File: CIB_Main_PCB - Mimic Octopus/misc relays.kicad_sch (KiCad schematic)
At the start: 7 parts, among them U3 ULN2803A, U4 MCP23017_SO, U6 ULN2803A, U7 MCP23017_SO, U8 ULN2803A

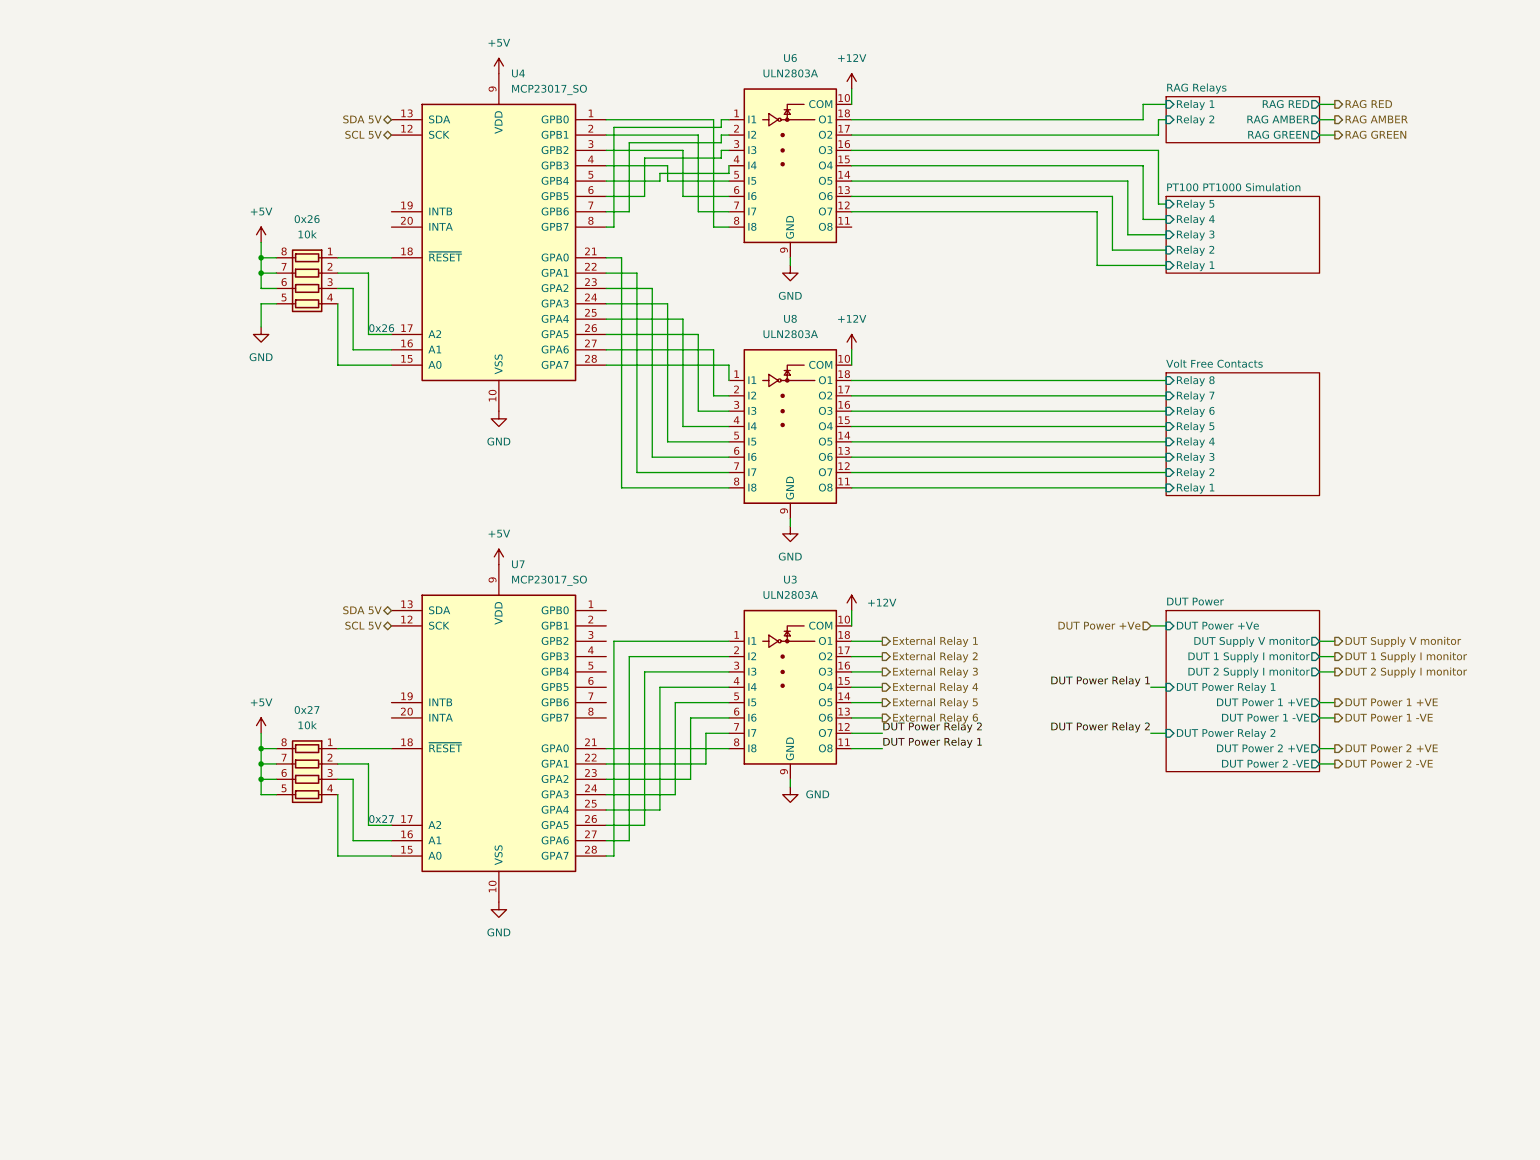
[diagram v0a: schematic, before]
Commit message: added version resistors
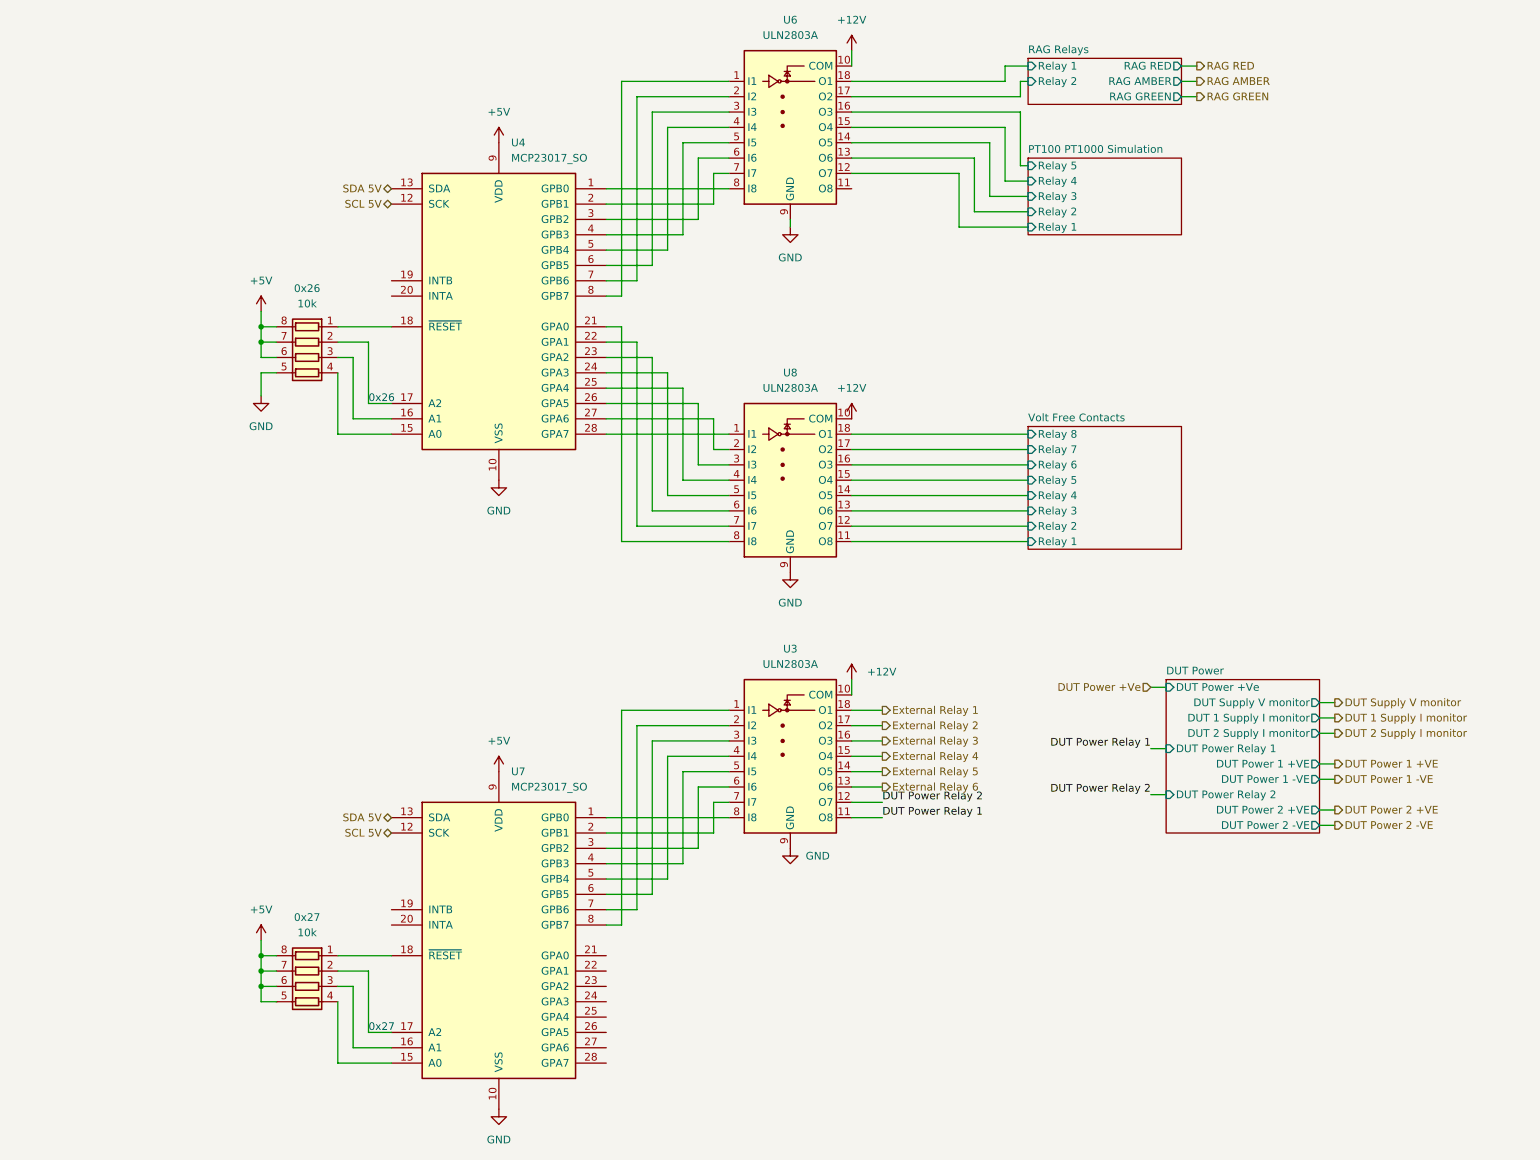
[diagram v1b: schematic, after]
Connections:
- net at U7.1 (GPB0): now also U3.8 (I8)
- net at U7.2 (GPB1): now also U3.7 (I7)
- net at U7.21 (GPA0): no longer U3.8 (I8)
- net at U7.22 (GPA1): no longer U3.7 (I7)
- net at U7.23 (GPA2): no longer U3.6 (I6)
- net at U7.24 (GPA3): no longer U3.5 (I5)
- net at U7.25 (GPA4): no longer U3.4 (I4)
- net at U7.26 (GPA5): no longer U3.3 (I3)
- net at U7.27 (GPA6): no longer U3.2 (I2)
- net at U7.28 (GPA7): no longer U3.1 (I1)
- net at U7.3 (GPB2): now also U3.6 (I6)
- net at U7.4 (GPB3): now also U3.5 (I5)
- net at U7.5 (GPB4): now also U3.4 (I4)
- net at U7.6 (GPB5): now also U3.3 (I3)
- net at U7.7 (GPB6): now also U3.2 (I2)
- net at U7.8 (GPB7): now also U3.1 (I1)
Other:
- moved on the sheet: 0x26, 0x27, U3, U4, U6, U7, U8

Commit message: added changes
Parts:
- renumbered 0x26 to 0x1, 0x27 to 0x2, U6 to U3, U8 to U5, U3 to U6
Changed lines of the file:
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@@
   (symbol (lib_id "Device:R_Pack04") (at 67.31 175.26 90) (mirror x) (unit 1)
     (in_bom yes) (on_board yes) (fields_autoplaced)
-    (property "Reference" "0x27" (id 0) (at 67.31 163.83 90))
+    (property "Reference" "0x2" (id 0) (at 67.31 163.83 90))
     (property "Value" "10k" (id 1) (at 67.31 166.37 90))
     (property "Footprint" "Resistor_SMD:R_Array_Convex_4x1206" (id 2) (at 67.31 182.245 90)
@@
   (symbol (lib_id "power:+12V") (at 157.48 81.28 0) (unit 1)
     (in_bom yes) (on_board yes) (fields_autoplaced)
-    (property "Reference" "#PWR097" (id 0) (at 157.48 85.09 0)
+    (property "Reference" "#PWR084" (id 0) (at 157.48 85.09 0)
       (effects (font (size 1.27 1.27)) hide)
     )
@@
   (symbol (lib_id "power:GND") (at 59.69 77.47 0) (unit 1)
     (in_bom yes) (on_board yes) (fields_autoplaced)
-    (property "Reference" "#PWR0117" (id 0) (at 59.69 83.82 0)
+    (property "Reference" "#PWR083" (id 0) (at 59.69 83.82 0)
       (effects (font (size 1.27 1.27)) hide)
     )
@@
   (symbol (lib_id "Transistor_Array:ULN2803A") (at 147.32 88.9 0) (unit 1)
     (in_bom yes) (on_board yes) (fields_autoplaced)
-    (property "Reference" "U8" (id 0) (at 147.32 73.66 0))
+    (property "Reference" "U5" (id 0) (at 147.32 73.66 0))
     (property "Value" "ULN2803A" (id 1) (at 147.32 76.2 0))
     (property "Footprint" "Package_DIP:DIP-18_W7.62mm_LongPads" (id 2) (at 148.59 105.41 0)
@@
   (symbol (lib_id "Device:R_Pack04") (at 67.31 71.12 90) (mirror x) (unit 1)
     (in_bom yes) (on_board yes) (fields_autoplaced)
-    (property "Reference" "0x26" (id 0) (at 67.31 59.69 90))
+    (property "Reference" "0x1" (id 0) (at 67.31 59.69 90))
     (property "Value" "10k" (id 1) (at 67.31 62.23 90))
     (property "Footprint" "Resistor_SMD:R_Array_Convex_4x1206" (id 2) (at 67.31 78.105 90)
@@
   (symbol (lib_id "Transistor_Array:ULN2803A") (at 147.32 30.48 0) (unit 1)
     (in_bom yes) (on_board yes) (fields_autoplaced)
-    (property "Reference" "U6" (id 0) (at 147.32 15.24 0))
+    (property "Reference" "U3" (id 0) (at 147.32 15.24 0))
     (property "Value" "ULN2803A" (id 1) (at 147.32 17.78 0))
     (property "Footprint" "Package_DIP:DIP-18_W7.62mm_LongPads" (id 2) (at 148.59 46.99 0)
@@
   (symbol (lib_id "power:+5V") (at 99.06 35.56 0) (unit 1)
     (in_bom yes) (on_board yes) (fields_autoplaced)
-    (property "Reference" "#PWR0112" (id 0) (at 99.06 39.37 0)
+    (property "Reference" "#PWR080" (id 0) (at 99.06 39.37 0)
       (effects (font (size 1.27 1.27)) hide)
     )
@@
   (symbol (lib_id "power:GND") (at 147.32 49.53 0) (unit 1)
     (in_bom yes) (on_board yes) (fields_autoplaced)
-    (property "Reference" "#PWR094" (id 0) (at 147.32 55.88 0)
+    (property "Reference" "#PWR081" (id 0) (at 147.32 55.88 0)
       (effects (font (size 1.27 1.27)) hide)
     )
@@
   (symbol (lib_id "power:GND") (at 99.06 195.58 0) (unit 1)
     (in_bom yes) (on_board yes) (fields_autoplaced)
-    (property "Reference" "#PWR0114" (id 0) (at 99.06 201.93 0)
+    (property "Reference" "#PWR091" (id 0) (at 99.06 201.93 0)
       (effects (font (size 1.27 1.27)) hide)
     )
@@
   (symbol (lib_id "power:+12V") (at 157.48 20.32 0) (unit 1)
     (in_bom yes) (on_board yes) (fields_autoplaced)
-    (property "Reference" "#PWR085" (id 0) (at 157.48 24.13 0)
+    (property "Reference" "#PWR079" (id 0) (at 157.48 24.13 0)
       (effects (font (size 1.27 1.27)) hide)
     )
@@
   (symbol (lib_id "power:+5V") (at 99.06 139.7 0) (unit 1)
     (in_bom yes) (on_board yes)
-    (property "Reference" "#PWR0116" (id 0) (at 99.06 143.51 0)
+    (property "Reference" "#PWR088" (id 0) (at 99.06 143.51 0)
       (effects (font (size 1.27 1.27)) hide)
     )
@@
   (symbol (lib_id "power:+5V") (at 59.69 167.64 0) (unit 1)
     (in_bom yes) (on_board yes)
-    (property "Reference" "#PWR0113" (id 0) (at 59.69 171.45 0)
+    (property "Reference" "#PWR090" (id 0) (at 59.69 171.45 0)
       (effects (font (size 1.27 1.27)) hide)
     )
@@
   (symbol (lib_id "Transistor_Array:ULN2803A") (at 147.32 134.62 0) (unit 1)
     (in_bom yes) (on_board yes) (fields_autoplaced)
-    (property "Reference" "U3" (id 0) (at 147.32 119.38 0))
+    (property "Reference" "U6" (id 0) (at 147.32 119.38 0))
     (property "Value" "ULN2803A" (id 1) (at 147.32 121.92 0))
     (property "Footprint" "Package_DIP:DIP-18_W7.62mm_LongPads" (id 2) (at 148.59 151.13 0)
@@
   (symbol (lib_id "power:GND") (at 147.32 152.4 0) (unit 1)
     (in_bom yes) (on_board yes) (fields_autoplaced)
-    (property "Reference" "#PWR0375" (id 0) (at 147.32 158.75 0)
+    (property "Reference" "#PWR089" (id 0) (at 147.32 158.75 0)
       (effects (font (size 1.27 1.27)) hide)
     )
@@
   (symbol (lib_id "power:GND") (at 99.06 91.44 0) (unit 1)
     (in_bom yes) (on_board yes) (fields_autoplaced)
-    (property "Reference" "#PWR0115" (id 0) (at 99.06 97.79 0)
+    (property "Reference" "#PWR085" (id 0) (at 99.06 97.79 0)
       (effects (font (size 1.27 1.27)) hide)
     )
@@
   (symbol (lib_id "power:+5V") (at 59.69 63.5 0) (unit 1)
     (in_bom yes) (on_board yes)
-    (property "Reference" "#PWR0121" (id 0) (at 59.69 67.31 0)
+    (property "Reference" "#PWR082" (id 0) (at 59.69 67.31 0)
       (effects (font (size 1.27 1.27)) hide)
     )
@@
   (symbol (lib_id "power:+12V") (at 157.48 124.46 0) (unit 1)
     (in_bom yes) (on_board yes) (fields_autoplaced)
-    (property "Reference" "#PWR0374" (id 0) (at 157.48 128.27 0)
+    (property "Reference" "#PWR087" (id 0) (at 157.48 128.27 0)
       (effects (font (size 1.27 1.27)) hide)
     )
@@
   (symbol (lib_id "power:GND") (at 147.32 106.68 0) (unit 1)
     (in_bom yes) (on_board yes) (fields_autoplaced)
-    (property "Reference" "#PWR0101" (id 0) (at 147.32 113.03 0)
-      (effects (font (size 1.27 1.27)) hide)
-    )
+    (property "Reference" "#PWR086" (id 0) (at 147.32 113.03 0)
+      (effects (font (size 1.27 1.27)) hide)
+    )

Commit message: V0.1 PCB to be sent out
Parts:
- removed 0x1, 0x2: 10k, Resistor_SMD:R_Array_Convex_4x1206, symbol Device:R_Pack04
- removed U4, U7: MCP23017_SO, Package_SO:SOIC-28W_7.5x17.9mm_P1.27mm, symbol Interface_Expansion:MCP23017_SO
- added U4, U7, U8: 74HC595, Package_DIP:DIP-16_W7.62mm_LongPads, symbol 74xx:74HC595
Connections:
- net +5V: now also U4.10 (~{SRCLR}), U4.16 (VCC), U7.10 (~{SRCLR}), U7.16 (VCC), U8.10 (~{SRCLR}), U8.16 (VCC)
- net DUT Power Relay 1: now also U3.11 (O8); no longer U6.11 (O8)
- net DUT Power Relay 2: now also U3.12 (O7); no longer U6.12 (O7)
- net External Relay 1: now also U6.16 (O3); no longer U6.18 (O1)
- net External Relay 2: now also U6.15 (O4); no longer U6.17 (O2)
- net External Relay 3: now also U6.14 (O5); no longer U6.16 (O3)
- net External Relay 4: now also U6.13 (O6); no longer U6.15 (O4)
- net External Relay 5: now also U6.12 (O7); no longer U6.14 (O5)
- net External Relay 6: now also U6.11 (O8); no longer U6.13 (O6)
- net GND: now also U4.13 (~{OE}), U4.8 (GND), U7.13 (~{OE}), U7.8 (GND), U8.13 (~{OE}), U8.8 (GND)
- net PT100 PT1000 Simulation/Relay 1: now also U3.16 (O3); no longer U3.12 (O7)
- net PT100 PT1000 Simulation/Relay 2: now also U3.17 (O2); no longer U3.13 (O6)
- net PT100 PT1000 Simulation/Relay 3: now also U3.15 (O4); no longer U3.14 (O5)
- net PT100 PT1000 Simulation/Relay 4: now also U3.14 (O5); no longer U3.15 (O4)
- net PT100 PT1000 Simulation/Relay 5: now also U3.13 (O6); no longer U3.16 (O3)
- net RAG Relays/Relay 1: now also U6.17 (O2); no longer U3.18 (O1)
- net RAG Relays/Relay 2: now also U6.18 (O1); no longer U3.17 (O2)
- net at U5.1 (I1): now also U7.7 (QH)
- net at U5.2 (I2): now also U7.6 (QG)
- net at U5.3 (I3): now also U7.5 (QF)
- net at U5.4 (I4): now also U7.4 (QE)
- net at U5.5 (I5): now also U7.3 (QD)
- net at U5.6 (I6): now also U7.2 (QC)
- net at U5.7 (I7): now also U7.1 (QB)
- net at U5.8 (I8): now also U7.15 (QA)
- net at U6.8 (I8): now also U8.15 (QA)
- net at U6.7 (I7): now also U8.1 (QB)
- net at U6.6 (I6): now also U8.2 (QC)
- net at U6.5 (I5): now also U8.3 (QD)
- net at U6.4 (I4): now also U8.4 (QE)
- net at U6.3 (I3): now also U8.5 (QF)
- net at U6.2 (I2): now also U8.6 (QG)
- net at U6.1 (I1): now also U8.7 (QH)
- net at U3.1 (I1): now also U4.7 (QH)
- net at U3.2 (I2): now also U4.6 (QG)
- net at U3.3 (I3): now also U4.5 (QF)
- net at U3.4 (I4): now also U4.4 (QE)
- net at U3.5 (I5): now also U4.3 (QD)
- net at U3.6 (I6): now also U4.2 (QC)
- net at U3.7 (I7): now also U4.1 (QB)
- net at U3.8 (I8): now also U4.15 (QA)
- new net: U7.9 (QH'), U8.14 (SER)
- new net Clock: U4.11 (SRCLK), U7.11 (SRCLK), U8.11 (SRCLK)
- new net DIN: U7.14 (SER)
- new net DOUT: U4.9 (QH')
- new net External Relay 7: U3.18 (O1)
- new net Latch: U4.12 (RCLK), U7.12 (RCLK), U8.12 (RCLK)
- new net data: U4.14 (SER), U8.9 (QH')
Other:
- note removed: "0x26"
- note removed: "0x27"
- moved on the sheet: U3, U5, U6

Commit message: BoM
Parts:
- U3, U5, U6: Height (none) -> 5; Mouser # (none) -> 511-ULN2803A; Mouser Part Number 511-ULN2803A -> (none)
- U4, U7, U8: Height (none) -> 5
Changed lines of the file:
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@@
+      (effects (font (size 1.27 1.27)) hide)
+    )
+    (property "Manufacturer" "STMicroelectronics" (id 7) (at 85.09 106.68 0)
+      (effects (font (size 1.27 1.27)) hide)
+    )
+    (property "Manufacturer #" "ULN2803A" (id 5) (at 85.09 106.68 0)
       (effects (font (size 1.27 1.27)) hide)
     )
@@
       (effects (font (size 1.27 1.27)) hide)
     )
-    (property "Manufacturer #" "ULN2803A" (id 5) (at 85.09 106.68 0)
-      (effects (font (size 1.27 1.27)) hide)
-    )
-    (property "Manufacturere" "" (id 6) (at 85.09 106.68 0)
-      (effects (font (size 1.27 1.27)) hide)
-    )
-    (property "Manufacturer" "STMicroelectronics" (id 7) (at 85.09 106.68 0)
-      (effects (font (size 1.27 1.27)) hide)
-    )
-    (property "Mouser #" "" (id 8) (at 85.09 106.68 0)
-      (effects (font (size 1.27 1.27)) hide)
-    )
-    (property "Mouser Part Number" "511-ULN2803A" (id 9) (at 85.09 106.68 0)
+    (property "Mouser #" "511-ULN2803A" (id 8) (at 85.09 106.68 0)
+      (effects (font (size 1.27 1.27)) hide)
+    )
+    (property "Mouser Part Number" "" (id 9) (at 85.09 106.68 0)
+      (effects (font (size 1.27 1.27)) hide)
+    )
+    (property "Height" "5" (id 10) (at 85.09 106.68 0)
       (effects (font (size 1.27 1.27)) hide)
     )
@@
       (effects (font (size 1.27 1.27)) hide)
     )
+    (property "Manufacturer" "STMicroelectronics" (id 7) (at 85.09 48.26 0)
+      (effects (font (size 1.27 1.27)) hide)
+    )
+    (property "Manufacturer #" "ULN2803A" (id 5) (at 85.09 48.26 0)
+      (effects (font (size 1.27 1.27)) hide)
+    )
     (property "DigiKey #" "497-2356-5-ND" (id 4) (at 85.09 48.26 0)
       (effects (font (size 1.27 1.27)) hide)
     )
-    (property "Manufacturer #" "ULN2803A" (id 5) (at 85.09 48.26 0)
-      (effects (font (size 1.27 1.27)) hide)
-    )
-    (property "Manufacturere" "" (id 6) (at 85.09 48.26 0)
-      (effects (font (size 1.27 1.27)) hide)
-    )
-    (property "Manufacturer" "STMicroelectronics" (id 7) (at 85.09 48.26 0)
-      (effects (font (size 1.27 1.27)) hide)
-    )
-    (property "Mouser #" "" (id 8) (at 85.09 48.26 0)
-      (effects (font (size 1.27 1.27)) hide)
-    )
-    (property "Mouser Part Number" "511-ULN2803A" (id 9) (at 85.09 48.26 0)
+    (property "Mouser #" "511-ULN2803A" (id 8) (at 85.09 48.26 0)
+      (effects (font (size 1.27 1.27)) hide)
+    )
+    (property "Mouser Part Number" "" (id 9) (at 85.09 48.26 0)
+      (effects (font (size 1.27 1.27)) hide)
+    )
+    (property "Height" "5" (id 10) (at 85.09 48.26 0)
       (effects (font (size 1.27 1.27)) hide)
     )
@@
       (effects (font (size 1.27 1.27)) hide)
     )
+    (property "Height" "5" (id 4) (at 44.45 93.98 0)
+      (effects (font (size 1.27 1.27)) hide)
+    )
     (pin "1")
     (pin "10")
@@
       (effects (font (size 1.27 1.27)) hide)
     )
+    (property "Height" "5" (id 4) (at 44.45 35.56 0)
+      (effects (font (size 1.27 1.27)) hide)
+    )
     (pin "1")
     (pin "10")
@@
     )
     (property "Datasheet" "http://www.ti.com/lit/ds/symlink/sn74hc595.pdf" (id 3) (at 44.45 143.51 0)
+      (effects (font (size 1.27 1.27)) hide)
+    )
+    (property "Height" "5" (id 4) (at 44.45 143.51 0)
       (effects (font (size 1.27 1.27)) hide)
     )
@@
       (effects (font (size 1.27 1.27)) hide)
     )
+    (property "Manufacturer" "STMicroelectronics" (id 7) (at 85.09 156.21 0)
+      (effects (font (size 1.27 1.27)) hide)
+    )
+    (property "Manufacturer #" "ULN2803A" (id 5) (at 85.09 156.21 0)
+      (effects (font (size 1.27 1.27)) hide)
+    )
     (property "DigiKey #" "497-2356-5-ND" (id 4) (at 85.09 156.21 0)
       (effects (font (size 1.27 1.27)) hide)
     )
-    (property "Manufacturer #" "ULN2803A" (id 5) (at 85.09 156.21 0)
-      (effects (font (size 1.27 1.27)) hide)
-    )
-    (property "Manufacturere" "" (id 6) (at 85.09 156.21 0)
-      (effects (font (size 1.27 1.27)) hide)
-    )
-    (property "Manufacturer" "STMicroelectronics" (id 7) (at 85.09 156.21 0)
-      (effects (font (size 1.27 1.27)) hide)
-    )
-    (property "Mouser #" "" (id 8) (at 85.09 156.21 0)
-      (effects (font (size 1.27 1.27)) hide)
-    )
-    (property "Mouser Part Number" "511-ULN2803A" (id 9) (at 85.09 156.21 0)
-      (effects (font (size 1.27 1.27)) hide)
-    )
+    (property "Mouser #" "511-ULN2803A" (id 8) (at 85.09 156.21 0)
+      (effects (font (size 1.27 1.27)) hide)
+    )
+    (property "Mouser Part Number" "" (id 9) (at 85.09 156.21 0)
+      (effects (font (size 1.27 1.27)) hide)
+    )
+    (property "Height" "5" (id 10) (at 85.09 156.21 0)
+      (effects (font (size 1.27 1.27)) hide)
+    )

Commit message: changes
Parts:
- removed U6: ULN2803A, Package_DIP:DIP-18_W7.62mm_LongPads, symbol Transistor_Array:ULN2803A
- added Q1, Q2, Q3, Q4, Q5, Q6, Q7, Q8: RS1G, Package_TO_SOT_SMD:SOT-23, symbol Transistor_FET:BS870
- U5: footprint Package_DIP:DIP-18_W7.62mm_LongPads -> Package_SO:SOIC-16W_7.5x12.8mm_P1.27mm
- U8: footprint Package_DIP:DIP-16_W7.62mm_LongPads -> Package_SO:SOIC-16_3.9x9.9mm_P1.27mm
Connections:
- net External Relay 1: now also Q3.3 (D)
- net GND: now also Q1.2 (S), Q2.2 (S), Q3.2 (S), Q4.2 (S), Q5.2 (S), Q6.2 (S), Q7.2 (S), Q8.2 (S)
- net RAG Relays/Relay 1: now also Q2.3 (D)
- net RAG Relays/Relay 2: now also Q1.3 (D)
- net at U8.4 (QE): now also Q4.1 (G)
- net at U8.5 (QF): now also Q3.1 (G)
- net at U8.6 (QG): now also Q2.1 (G)
- net at U8.7 (QH): now also Q1.1 (G)
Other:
- sheet DUT Power ports: added none; removed DUT Power 1 +VE, DUT Power 1 -VE, DUT Power 2 +VE, DUT Power 2 -VE
